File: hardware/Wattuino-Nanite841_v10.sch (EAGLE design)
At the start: 20 parts, among them IC1 ATTINY841-MU, J1 USB-MICRO, J2 MA07-1, J3 MA07-1, SW1 SW-TACTILE-PTS840P, X1 PASSER-07, X2 PASSER-07, X3 PASSER-07

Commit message: updated layout and schematics
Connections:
- net PA1: now also IC1.(PCINT1/ADC1/AIN00/TOCC0/TXD0/MOSI)PA1; no longer IC1.(PCINT1/ADC1/AIN00/TOCC09/TSC0/MOSI)PA1
- net PB0: now also IC1.(PCINT8/ADC11/XTAL1/CLKI)PB0; no longer IC1.(PCINT8/AEDC11/XTAL1/CLKI)PB0
- net PB2: now also IC1.(PCINT10/ADC8/CLKO/TOCC7/ICP2/RXD0)PB2; no longer IC1.(PCINT10/ADC8/CLK0/TOCC7/ICP2/RXD0)PB2
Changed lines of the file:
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@@
 <?xml version="1.0" encoding="utf-8"?>
 <!DOCTYPE eagle SYSTEM "eagle.dtd">
-<eagle version="7.3.0">
+<eagle version="7.5.0">
 <drawing>
 <settings>
@@
 <setting verticaltext="up"/>
 </settings>
-<grid distance="0.05" unitdist="inch" unit="inch" style="lines" multiple="1" display="yes" altdistance="0.025" altunitdist="inch" altunit="inch"/>
+<grid distance="0.1" unitdist="inch" unit="inch" style="lines" multiple="1" display="no" altdistance="0.01" altunitdist="inch" altunit="inch"/>
 <layers>
 <layer number="1" name="Top" color="4" fill="1" visible="no" active="no"/>
@@
 <segment>
 <wire x1="113.03" y1="107.95" x2="147.32" y2="107.95" width="0.1524" layer="91"/>
-<pinref part="IC1" gate="IC" pin="(PCINT8/AEDC11/XTAL1/CLKI)PB0"/>
+<pinref part="IC1" gate="IC" pin="(PCINT8/ADC11/XTAL1/CLKI)PB0"/>
 <pinref part="R3" gate="R" pin="1"/>
 <label x="132.08" y="107.95" size="1.27" layer="95"/>
@@
 <net name="PB2" class="0">
 <segment>
-<pinref part="IC1" gate="IC" pin="(PCINT10/ADC8/CLK0/TOCC7/ICP2/RXD0)PB2"/>
+<pinref part="IC1" gate="IC" pin="(PCINT10/ADC8/CLKO/TOCC7/ICP2/RXD0)PB2"/>
 <wire x1="113.03" y1="102.87" x2="137.16" y2="102.87" width="0.1524" layer="91"/>
 <pinref part="LED" gate="D" pin="C"/>
@@
 <net name="PA1" class="0">
 <segment>
-<pinref part="IC1" gate="IC" pin="(PCINT1/ADC1/AIN00/TOCC09/TSC0/MOSI)PA1"/>
+<pinref part="IC1" gate="IC" pin="(PCINT1/ADC1/AIN00/TOCC0/TXD0/MOSI)PA1"/>
 <wire x1="113.03" y1="128.27" x2="124.46" y2="128.27" width="0.1524" layer="91"/>
 <label x="124.46" y="128.27" size="1.27" layer="95" xref="yes"/>

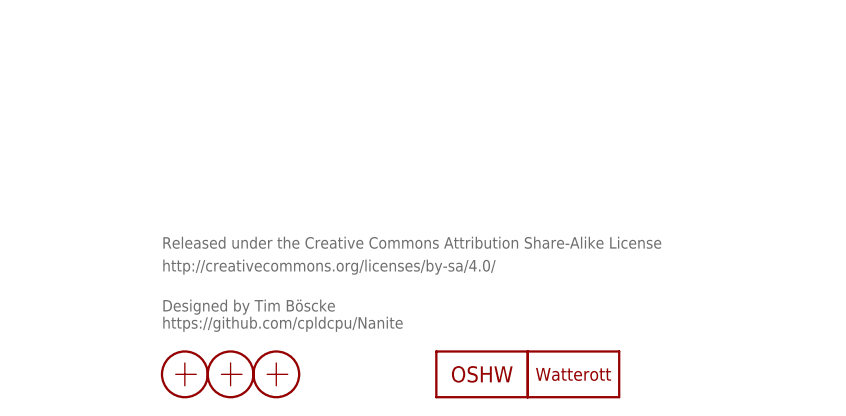
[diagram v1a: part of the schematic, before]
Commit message: updated schematics
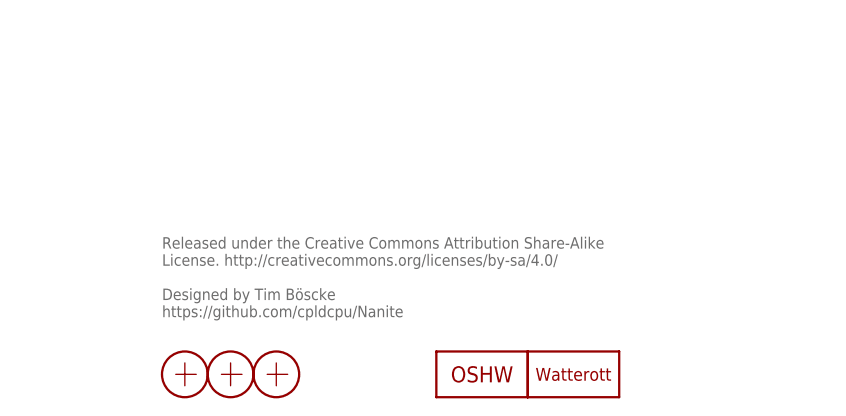
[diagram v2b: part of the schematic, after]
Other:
- note added: "Released under the Creative Commons Attribution Share-Alike License. http://creativecommons.org/licenses/by-sa/4.0/ Designed by Tim Böscke https://github.com/cpldcpu/Nanite"
- note removed: "Designed by Tim Böscke https://github.com/cpldcpu/Nanite"
- note removed: "Released under the Creative Commons Attribution Share-Alike License"
- note removed: "http://creativecommons.org/licenses/by-sa/4.0/"
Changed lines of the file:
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@@
 <setting verticaltext="up"/>
 </settings>
-<grid distance="0.1" unitdist="inch" unit="inch" style="lines" multiple="1" display="no" altdistance="0.01" altunitdist="inch" altunit="inch"/>
+<grid distance="0.05" unitdist="inch" unit="inch" style="lines" multiple="1" display="yes" altdistance="0.025" altunitdist="inch" altunit="inch"/>
 <layers>
 <layer number="1" name="Top" color="4" fill="1" visible="no" active="no"/>
@@
 <sheet>
 <plain>
-<text x="162.56" y="21.59" size="1.27" layer="95">Released under the Creative Commons Attribution Share-Alike License</text>
-<text x="162.56" y="19.05" size="1.27" layer="95">http://creativecommons.org/licenses/by-sa/4.0/</text>
-<text x="162.56" y="12.7" size="1.27" layer="95">Designed by Tim Böscke
+<text x="162.56" y="22.86" size="1.27" layer="95" align="top-left">Released under the Creative Commons Attribution Share-Alike
+License. http://creativecommons.org/licenses/by-sa/4.0/
+Designed by Tim Böscke
 https://github.com/cpldcpu/Nanite</text>
 <wire x1="189.865" y1="102.87" x2="191.135" y2="102.87" width="0.4064" layer="94"/>

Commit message: updated schematics
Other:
- note added: "ISP-MISO"
- note added: "ISP-MOSI"
- note added: "ISP-SCK"
- note added: "Pin | Map 1 | Map 2 ------------------- PA0 | D0 | D10 PA1 | D1 | D9 PA2 | D2 | D8 PA3 | D3 | D7 PA4 | D4 | D6 PA5 | D5 | D5 PA6 | D6 | D4 PA7 | D7 | D3 PB0 | D10 | D0 PB1 | D9 | D1 PB2 | D8 | D2 Map 1 = David A. Mellis - https://github.com/damellis/attiny Map 2 = Spence Konde - https://github.com/SpenceKonde/ATTinyCore"
- note added: "RESET"
- note added: "RST"
- note removed: "Arduino"
- note removed: "D11/RST"
- note removed: "RST/D11"
- moved on the sheet: J2, J3
